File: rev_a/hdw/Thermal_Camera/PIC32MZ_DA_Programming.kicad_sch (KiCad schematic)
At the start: 18 parts

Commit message: lots of schematic progress
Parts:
- C? (x2): footprint Capacitors_SMD:C_0603 -> (none); Digi-Key PN 1276-1935-1-ND -> (none); display_footprint 0603 -> (none)
- L? (x2): footprint Inductors_SMD:L_0603 -> (none); Digi-Key PN 490-1014-1-ND -> (none)
- R? (x2): footprint Resistors_SMD:R_0603 -> (none); Digi-Key PN 541-10.0HCT-ND -> (none); Wattage 1/10W -> (none); display_footprint 0603 -> (none)
- R? (x2): footprint Resistors_SMD:R_0603 -> (none); Digi-Key PN 541-10.0KHCT-ND -> (none); Wattage 1/10W -> (none); display_footprint 0603 -> (none)
- R?: footprint Resistors_SMD:R_0603 -> (none); Digi-Key PN 541-1.00KHCT-ND -> (none); Wattage 1/10W -> (none); display_footprint 0603 -> (none)
- gave numbers to parts that had none: 1

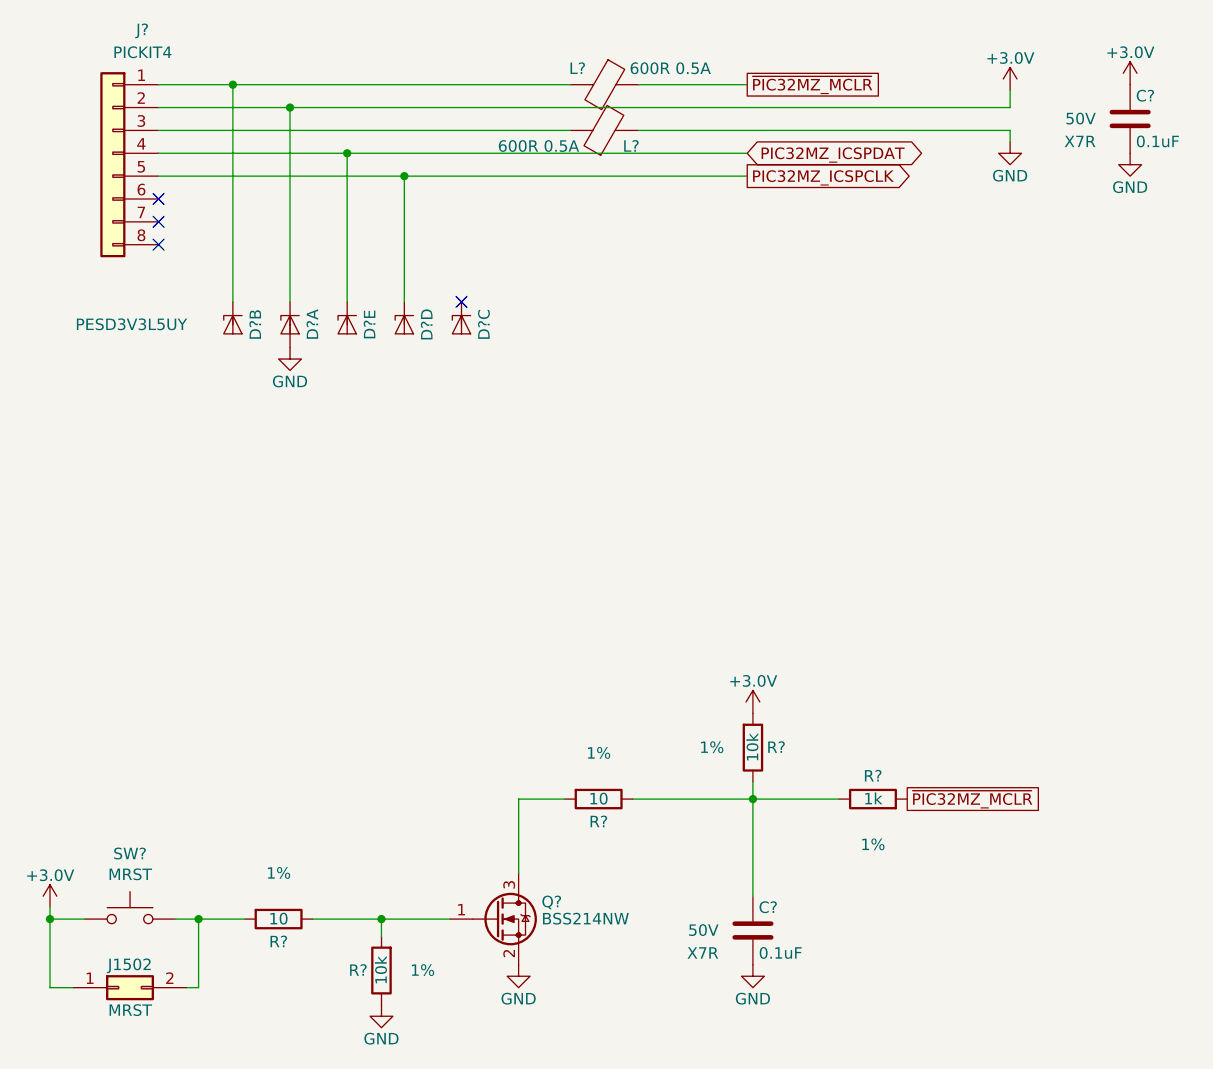
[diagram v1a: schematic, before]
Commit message: assigned a ton of footprints
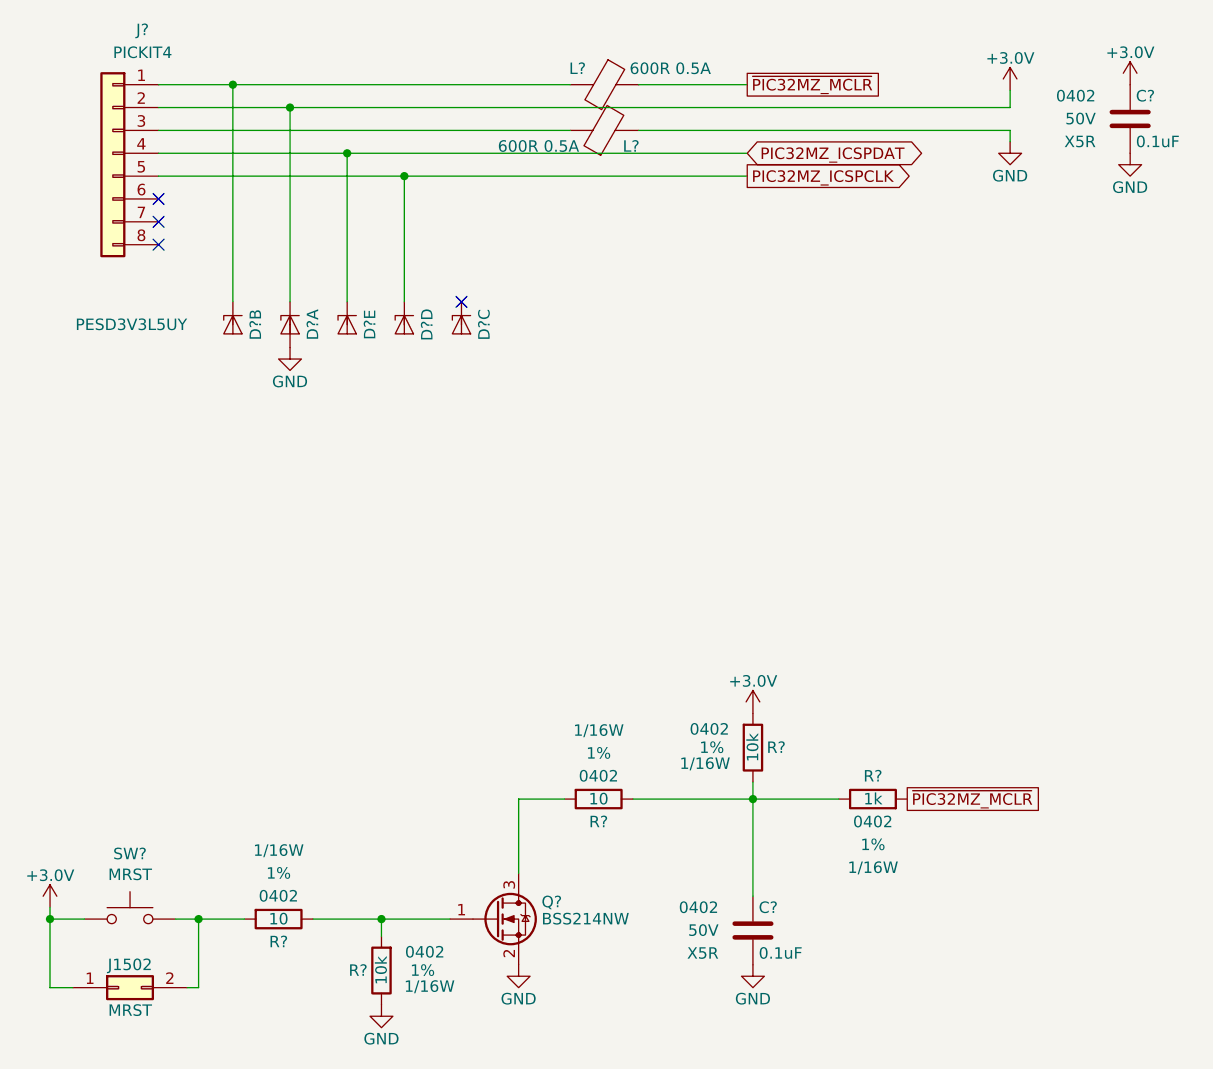
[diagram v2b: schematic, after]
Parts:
- C? (x2): footprint (none) -> Capacitors_SMD:C_0402; Dielectric X7R -> X5R; display_footprint (none) -> 0402
- J1502: footprint (none) -> Connector_PinHeader_2.54mm:PinHeader_1x02_P2.54mm_Vertical
- L? (x2): footprint (none) -> Inductors_SMD:L_0402
- R? (x5): footprint (none) -> Resistors_SMD:R_0402; Wattage (none) -> 1/16W; display_footprint (none) -> 0402
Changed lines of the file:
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@@
 			)
 		)
-		(property "Footprint" ""
+		(property "Footprint" "Resistors_SMD:R_0402"
 			(at 95.25 139.7 0)
 			(effects
@@
 			)
 		)
-		(property "display_footprint" ""
+		(property "display_footprint" "0402"
 			(at 95.25 137.16 90)
 			(effects
@@
 			)
 		)
-		(property "Wattage" ""
+		(property "Wattage" "1/16W"
 			(at 95.25 132.08 90)
 			(effects
@@
 			)
 		)
-		(property "Footprint" ""
+		(property "Footprint" "Inductors_SMD:L_0402"
 			(at 131.445 53.848 90)
 			(effects
@@
 			)
 		)
-		(property "Footprint" ""
+		(property "Footprint" "Resistors_SMD:R_0402"
 			(at 106.68 145.415 0)
 			(effects
@@
 			)
 		)
-		(property "display_footprint" ""
+		(property "display_footprint" "0402"
 			(at 111.506 143.383 0)
 			(effects
@@
 			)
 		)
-		(property "Wattage" ""
+		(property "Wattage" "1/16W"
 			(at 112.014 147.193 0)
 			(effects
@@
 			)
 		)
-		(property "Footprint" ""
+		(property "Footprint" "Capacitors_SMD:C_0402"
 			(at 190.8302 54.61 0)
 			(effects
@@
 			)
 		)
-		(property "display_footprint" ""
+		(property "display_footprint" "0402"
 			(at 186.055 48.26 0)
 			(effects
@@
 			)
 		)
-		(property "Dielectric" "X7R"
+		(property "Dielectric" "X5R"
 			(at 186.055 53.34 0)
 			(effects
@@
 			)
 		)
-		(property "Footprint" ""
+		(property "Footprint" "Resistors_SMD:R_0402"
 			(at 130.81 126.365 0)
 			(effects
@@
 			)
 		)
-		(property "display_footprint" ""
+		(property "display_footprint" "0402"
 			(at 130.81 123.825 90)
 			(effects
@@
 			)
 		)
-		(property "Wattage" ""
+		(property "Wattage" "1/16W"
 			(at 130.81 118.745 90)
 			(effects
@@
 			)
 		)
-		(property "Footprint" ""
+		(property "Footprint" "Capacitors_SMD:C_0402"
 			(at 148.9202 144.78 0)
 			(effects
@@
 			)
 		)
-		(property "display_footprint" ""
+		(property "display_footprint" "0402"
 			(at 144.145 138.43 0)
 			(effects
@@
 			)
 		)
-		(property "Dielectric" "X7R"
+		(property "Dielectric" "X5R"
 			(at 144.145 143.51 0)
 			(effects
@@
 			)
 		)
-		(property "Footprint" ""
+		(property "Footprint" "Resistors_SMD:R_0402"
 			(at 147.955 120.65 0)
 			(effects
@@
 			)
 		)
-		(property "display_footprint" ""
+		(property "display_footprint" "0402"
 			(at 143.129 118.618 0)
 			(effects
@@
 			)
 		)
-		(property "Wattage" ""
+		(property "Wattage" "1/16W"
 			(at 142.621 122.428 0)
 			(effects
@@
 			)
 		)
-		(property "Footprint" ""
+		(property "Footprint" "Connector_PinHeader_2.54mm:PinHeader_1x02_P2.54mm_Vertical"
 			(at 77.47 147.32 0)
 			(effects
@@
 			)
 		)
-		(property "Footprint" ""
+		(property "Footprint" "Resistors_SMD:R_0402"
 			(at 161.29 126.365 0)
 			(effects
@@
 			)
 		)
-		(property "display_footprint" ""
+		(property "display_footprint" "0402"
 			(at 161.29 128.905 90)
 			(effects
@@
 			)
 		)
-		(property "Wattage" ""
+		(property "Wattage" "1/16W"
 			(at 161.29 133.985 90)
 			(effects
@@
 			)
 		)
-		(property "Footprint" ""
+		(property "Footprint" "Inductors_SMD:L_0402"
 			(at 131.445 45.212 90)
 			(effects

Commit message: assigned some part numbers
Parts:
- C? (x2): Digi-Key PN (none) -> 490-10697-1-ND
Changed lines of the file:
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@@
 			)
 		)
-		(property "Digi-Key PN" ""
+		(property "Digi-Key PN" "490-10697-1-ND"
 			(at 200.66 38.1 0)
 			(effects
@@
 			)
 		)
-		(property "Digi-Key PN" ""
+		(property "Digi-Key PN" "490-10697-1-ND"
 			(at 158.75 128.27 0)
 			(effects

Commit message: assigned resistor part numbers
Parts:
- R? (x2): Digi-Key PN (none) -> RMCF0402FT10R0CT-ND
- R? (x2): Digi-Key PN (none) -> RMCF0402FT10K0CT-ND
- R?: Digi-Key PN (none) -> RMCF0402FT1K00CT-ND
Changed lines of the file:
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@@
 			)
 		)
-		(property "Digi-Key PN" ""
+		(property "Digi-Key PN" "RMCF0402FT10R0CT-ND"
 			(at 85.09 132.08 0)
 			(effects
@@
 			)
 		)
-		(property "Digi-Key PN" ""
+		(property "Digi-Key PN" "RMCF0402FT10K0CT-ND"
 			(at 114.3 135.255 0)
 			(effects
@@
 			)
 		)
-		(property "Digi-Key PN" ""
+		(property "Digi-Key PN" "RMCF0402FT10R0CT-ND"
 			(at 120.65 118.745 0)
 			(effects
@@
 			)
 		)
-		(property "Digi-Key PN" ""
+		(property "Digi-Key PN" "RMCF0402FT10K0CT-ND"
 			(at 140.335 110.49 0)
 			(effects
@@
 			)
 		)
-		(property "Digi-Key PN" ""
+		(property "Digi-Key PN" "RMCF0402FT1K00CT-ND"
 			(at 171.45 133.985 0)
 			(effects
